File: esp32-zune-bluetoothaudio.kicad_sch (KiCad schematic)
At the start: 20 parts

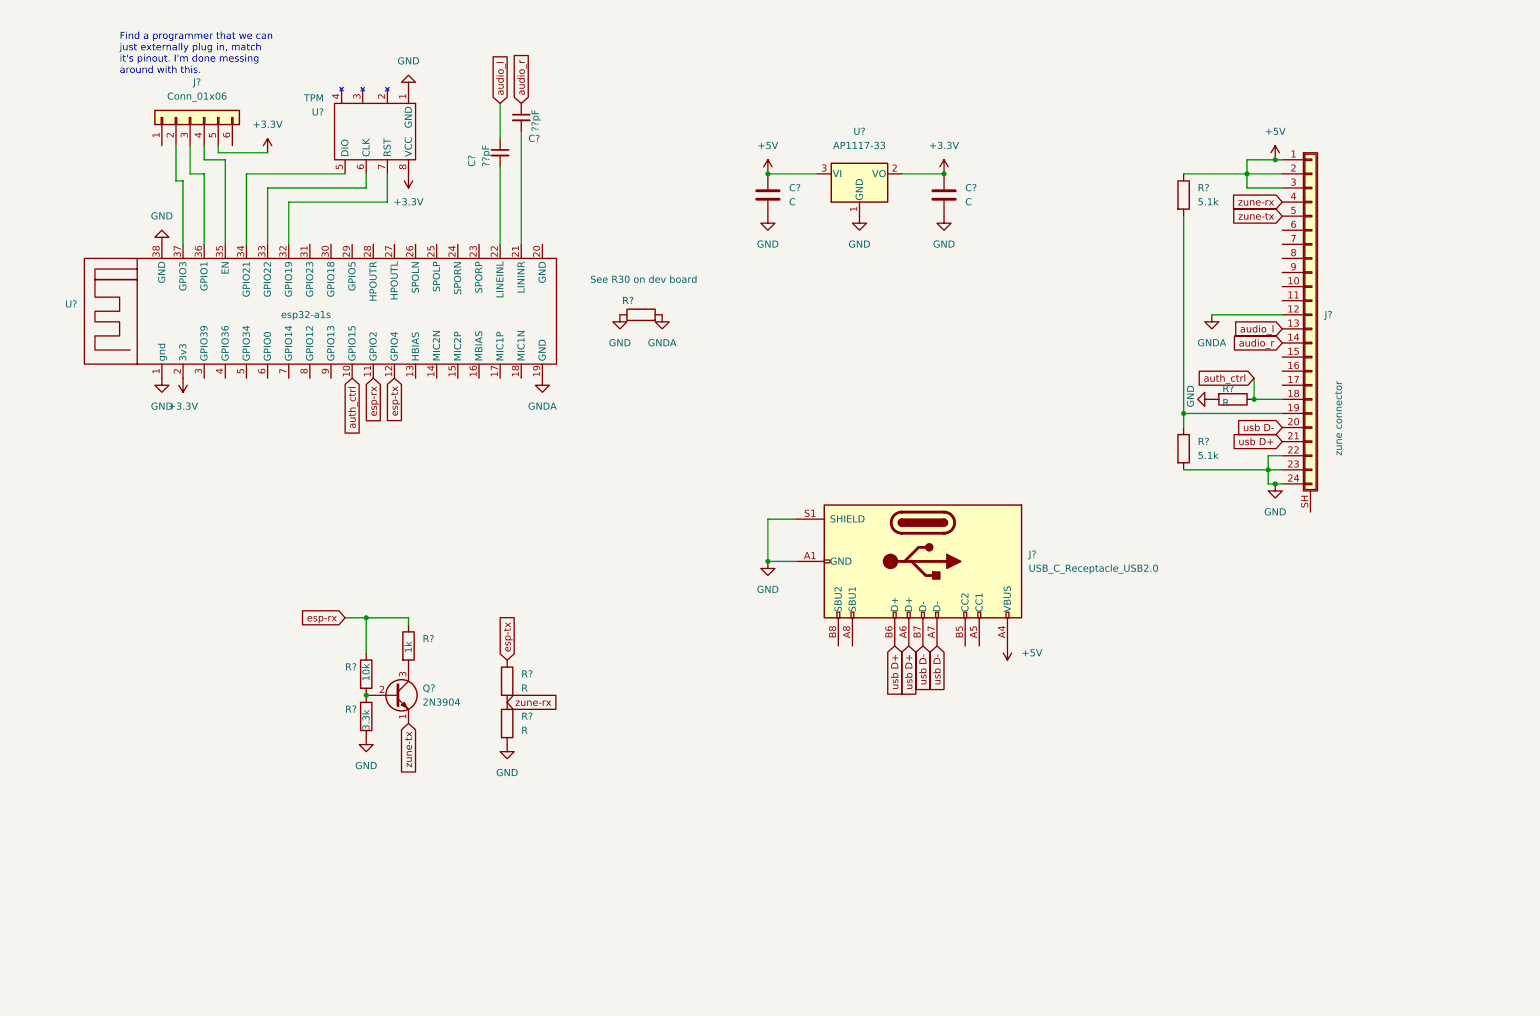
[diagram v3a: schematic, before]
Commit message: Symbols mostly associated, almost ready for PCB
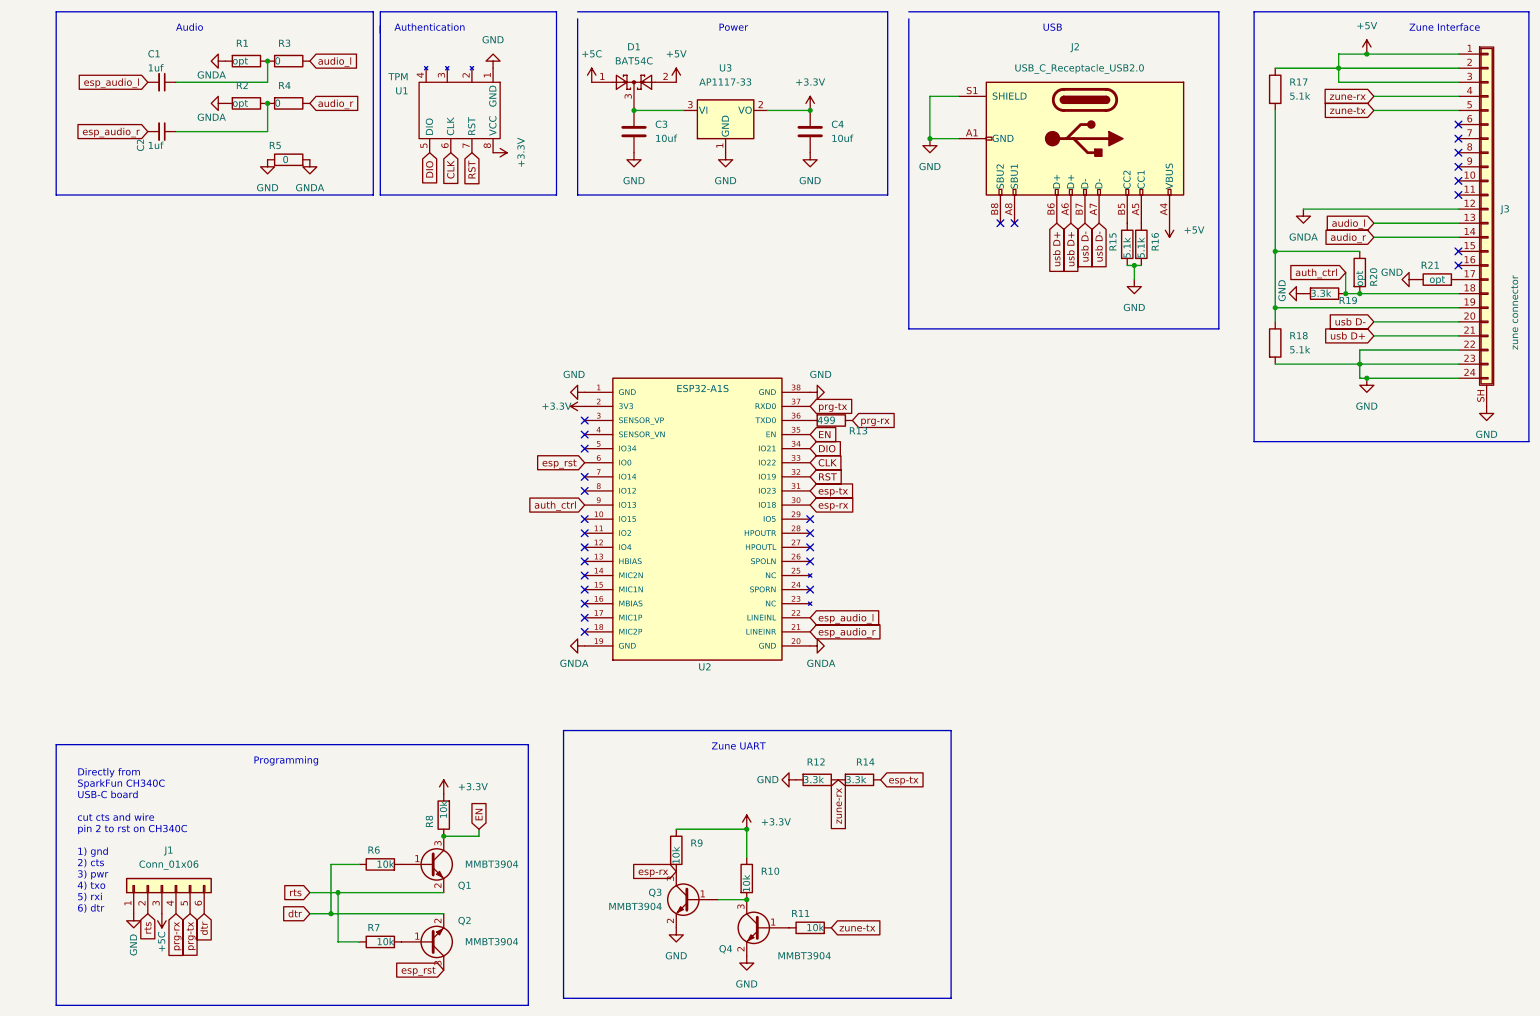
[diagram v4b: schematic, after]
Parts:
- removed Q?: 2N3904, Package_TO_SOT_THT:TO-92_Inline, symbol Transistor_BJT:2N3904
- removed R?: 3.3k, symbol Device:R
- removed R?: 1k, symbol Device:R
- removed R?: 10k, symbol Device:R
- removed U?: esp32-a1s, symbol esp32-zune-bluetoothaudio:esp32-a1s
- added D1: BAT54C, Package_TO_SOT_SMD:SOT-23, symbol Diode:BAT54C
- added Q1, Q2, Q3, Q4: MMBT3904, Package_TO_SOT_SMD:SOT-23, symbol Transistor_BJT:MMBT3904
- added R1, R2, R20, R21: opt, Resistor_SMD:R_0805_2012Metric_Pad1.20x1.40mm_HandSolder, symbol Device:R
- added R10, R11, R6, R7, R8, R9: 10k, Resistor_SMD:R_0805_2012Metric_Pad1.20x1.40mm_HandSolder, symbol Device:R
- added R13: 499, Resistor_SMD:R_0805_2012Metric_Pad1.20x1.40mm_HandSolder, symbol Device:R
- added R15, R16: 5.1k, Resistor_SMD:R_0805_2012Metric_Pad1.20x1.40mm_HandSolder, symbol Device:R
- added R3, R4: 0, Resistor_SMD:R_0805_2012Metric_Pad1.20x1.40mm_HandSolder, symbol Device:R
- added U2: ESP32-A1S, symbol esp32-zune-bluetoothaudio:ESP32-A1S
- C1, C2: renamed from C?; value ??pF -> 1uf; footprint (none) -> Capacitor_SMD:C_0805_2012Metric_Pad1.18x1.45mm_HandSolder
- C3, C4: renamed from C?; value C -> 10uf; footprint (none) -> Capacitor_SMD:C_0805_2012Metric_Pad1.18x1.45mm_HandSolder
- J1: renamed from J?; footprint (none) -> Connector_PinSocket_2.54mm:PinSocket_1x06_P2.54mm_Horizontal
- J2: renamed from J?; footprint (none) -> Connector_USB:USB_C_Receptacle_XKB_U262-16XN-4BVC11
- R12, R14, R19: renamed from R?; value R -> 3.3k; footprint (none) -> Resistor_SMD:R_0805_2012Metric_Pad1.20x1.40mm_HandSolder
- R17, R18: renamed from R?; footprint (none) -> Resistor_SMD:R_0805_2012Metric_Pad1.20x1.40mm_HandSolder
- R5: renamed from R?; value See R30 on dev board -> 0; footprint (none) -> Resistor_SMD:R_0805_2012Metric_Pad1.20x1.40mm_HandSolder
- U1: renamed from U?; footprint (none) -> Package_SO:Infineon_PG-DSO-8-27_3.9x4.9mm_EP2.65x3mm
- gave numbers to parts that had none: 2
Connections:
- net +3.3V: now also R10.1, R8.2, R9.1, U2.2 (3V3); no longer J1.5 (Pin_5)
- net +5V: now also D1.2; no longer C3.1, U3.3 (VI)
- net GND: now also J1.1 (Pin_1), J3.SH (Shield), Q3.2 (E), Q4.2 (E), R15.2, R16.2, R21.1, U2.1 (GND), U2.38 (GND)
- net GNDA: now also R1.2, R2.2, U2.19 (GND), U2.20 (GND)
- net audio_l: now also R3.1; no longer C1.1
- net audio_r: now also R4.1; no longer C2.1
- net auth_ctrl: now also R20.2, U2.9 (IO13)
- net esp-rx: now also Q3.3 (C), R9.2, U2.30 (IO18)
- net esp-tx: now also U2.31 (IO23)
- net zune-tx: now also R11.2
- net at J3.17 (Pin_17): now also R21.2
- net at J3.19 (Pin_19), R17.2, R18.1: now also R20.1
- net esp_audio_l: now reaches C1.2
- net esp_audio_l: now also U2.22 (LINEINL)
- net esp_audio_r: now reaches C2.2
- net esp_audio_r: now also U2.21 (LINEINR)
- net DIO: now reaches U1.5 (DIO)
- net DIO: now also U2.34 (IO21)
- net CLK: now reaches U1.6 (CLK)
- net CLK: now also U2.33 (IO22)
- net RST: now reaches U1.7 (RST)
- net RST: now also U2.32 (IO19)
- net rts: now reaches J1.2 (Pin_2)
- net rts: now also Q1.2 (E), R7.1
- net +5C: now reaches J1.3 (Pin_3)
- net +5C: now also D1.1
- net prg-rx: now reaches J1.4 (Pin_4)
- net prg-rx: now also R13.1
- net dtr: now reaches J1.6 (Pin_6)
- net dtr: now also Q2.2 (E), R6.1
- net at J2.A5 (CC1): now also R16.1
- net at J2.B5 (CC2): now also R15.1
- new net: C1.1, R1.1, R3.2
- new net: Q4.1 (B), R11.1
- new net: C2.1, R2.1, R4.2
- new net: Q2.1 (B), R7.2
- new net: C3.1, D1.3, U3.3 (VI)
- new net: Q1.1 (B), R6.2
- new net: Q3.1 (B), Q4.3 (C), R10.2
- new net: R13.2, U2.36 (TXD0)
- new net EN: Q1.3 (C), R8.1, U2.35 (EN)
- new net esp_rst: Q2.3 (C), U2.6 (IO0)
- new net prg-tx: J1.5 (Pin_5), U2.37 (RXD0)
- no-connect marks 0 -> 29
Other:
- note added: "Audio"
- note added: "Authentication"
- note added: "Directly from SparkFun CH340C USB-C board cut cts and wire pin 2 to rst on CH340C 1) gnd 2) cts 3) pwr 4) txo 5) rxi 6) dtr"
- note added: "Power"
- note added: "Programming"
- note added: "USB"
- note added: "Zune Interface"
- note added: "Zune UART"
- note removed: "Find a programmer that we can just externally plug in, match it's pinout. I'm done messing around with this."
- moved on the sheet: C1, C2, C3, C4, J1, J2, J3, R12, R14, R17, R18, R19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

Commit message: well... its a pcb without routing and its too big. gonna try to make it a two board layout, placing the esp32 behind the body of the zune.
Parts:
- J3: footprint (none) -> ZuneConnector:zune-edge-connector
- U2: footprint (none) -> ESP32-A1S:ESP32-A1S
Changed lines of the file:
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@@
       (effects (font (size 1.27 1.27)) (justify left))
     )
-    (property "Footprint" "" (id 2) (at 271.78 52.07 0)
+    (property "Footprint" "ZuneConnector:zune-edge-connector" (id 2) (at 271.78 52.07 0)
       (effects (font (size 1.27 1.27)) hide)
     )
@@
       (effects (font (size 1.27 1.27)) (justify right))
     )
-    (property "Footprint" "" (id 2) (at 114.3 77.47 0)
+    (property "Footprint" "ESP32-A1S:ESP32-A1S" (id 2) (at 114.3 77.47 0)
       (effects (font (size 1.27 1.27)) (justify left bottom) hide)
     )
@@
     )
     (path "/03c52831-5dc5-43c5-a442-8d23643b46fb"
-      (reference "J3") (unit 1) (value "zune connector") (footprint "")
+      (reference "J3") (unit 1) (value "zune connector") (footprint "ZuneConnector:zune-edge-connector")
     )
     (path "/a60336c2-b905-4375-92d6-e6d6e0e57614"
@@
     )
     (path "/e88eb51f-b9c8-4eb5-988e-2db0fca0b17d"
-      (reference "U2") (unit 1) (value "ESP32-A1S") (footprint "")
+      (reference "U2") (unit 1) (value "ESP32-A1S") (footprint "ESP32-A1S:ESP32-A1S")
     )
     (path "/5737e394-541e-4a6b-8517-1301aee4f642"

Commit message: layoutish
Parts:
- removed J3: zune connector, ZuneConnector:zune-edge-connector, symbol Connector_Generic_Shielded:Conn_01x24_Shielded
- added J3: Zune Passthrough, Connector_PinHeader_2.00mm:PinHeader_2x06_P2.00mm_Vertical_SMD, symbol Connector_Generic:Conn_02x06_Odd_Even
- J1: footprint Connector_PinSocket_2.54mm:PinSocket_1x06_P2.54mm_Horizontal -> Connector_PinHeader_2.54mm:PinHeader_1x06_P2.54mm_Vertical
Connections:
- net +5V: now also R17.2, R20.1, J3.1 (Pin_1); no longer R17.1
- net GND: now also R21.2, J3.6 (Pin_6); no longer R21.1
- net GNDA: now also J3.5 (Pin_5)
- net audio_l: now also J3.4 (Pin_4)
- net audio_r: now also J3.3 (Pin_3)
- net auth_ctrl: now also J3.11 (Pin_11)
- net usb D+: now also J3.10 (Pin_10)
- net usb D-: now also J3.9 (Pin_9)
- net zune-rx: now also J3.7 (Pin_7)
- net zune-tx: now also J3.8 (Pin_8)
- new net: J3.12 (Pin_12), R17.1, R18.1
- new net: J3.2 (Pin_2), R21.1
- no-connect marks 29 -> 21
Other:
- note added: "Pin mapping us) zune 1) 1-3 2) 17 3) 14 4) 13 5) 12 6) 22-24 7) 4 8) 5 9) 20 10) 21 11) 18 12) 19"
- moved on the sheet: R17, R18, R19, R20, R21
